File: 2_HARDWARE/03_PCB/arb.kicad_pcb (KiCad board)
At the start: 6 copper layers, 104.3 x 53.5 mm, 269 parts, among them J1 TYPE-C-31-M-12, J2 SMA, J3 SMA, J4 BNC, J5 PH-00244, SW1 TS-1187A-B-A-B, U1 TLV70333DBV, U10 LMK1C1103PWR, U11 STM32F446ZETx, U12 ICE40UP5K-SG48ITR, U13 93LC56BT-I_OT, U14 FT2232HL, U15 W25Q128JVSIQ, U16 W25Q128JVSIQ, U17 AD9850, U18 AD9744, U19 LM6171, U2 TLV76133DCY, U20 LM6171, U21 TMUX6104, U22 TPL0401B-10, U23 THS3491, U24 ADG1219BRJZ, U25 LM6171, U26 TMUX6104, U3 TLV70333DBV, U4 LM3880MF-1AA, U5 TLV70312DBV, U6 TLV70325DBV, U7 TPS65131RGE, U8 TPD2E001DRL, U9 ADG1219BRJZ, X1 ASE-10.000MHz, X2 ASE-100.000MHz, Y1 32.768k, Y2 12 MHz

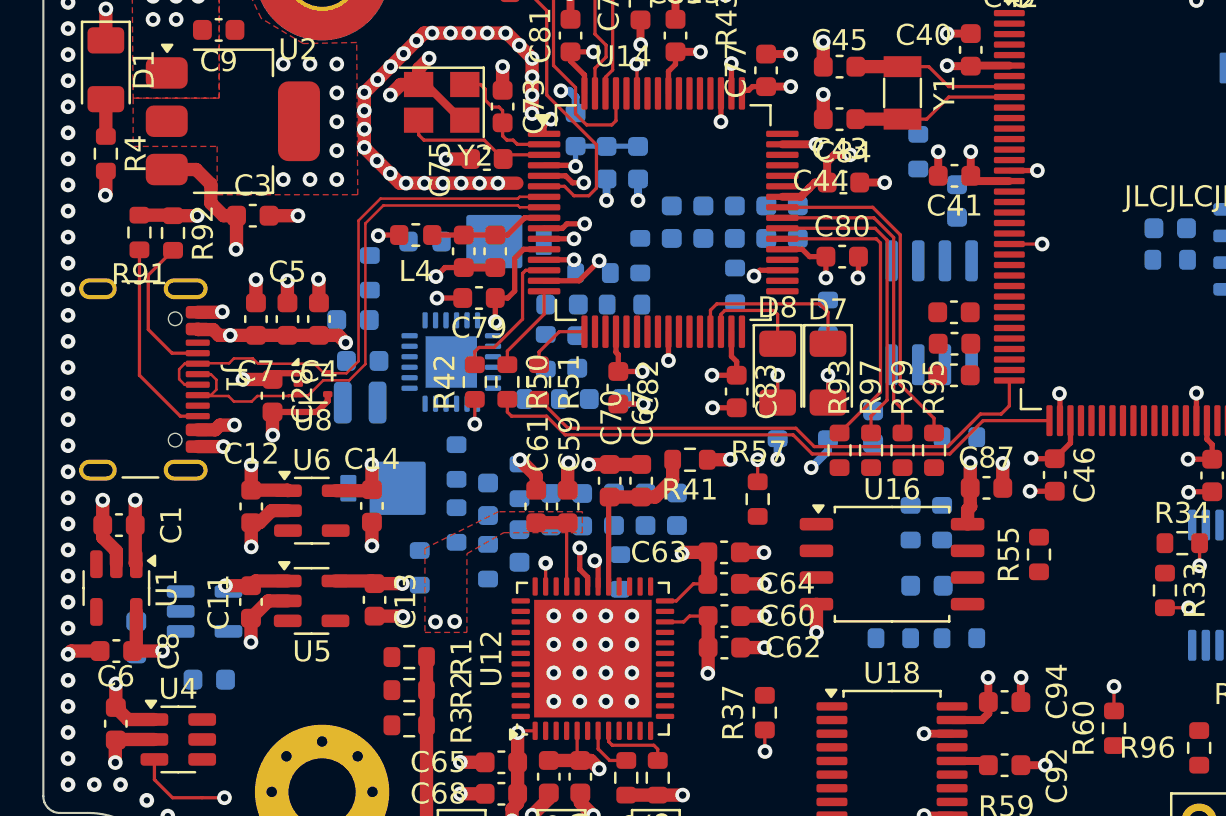
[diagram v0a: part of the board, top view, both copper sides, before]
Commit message: MINOR: Added missing vias, started on BS Routing.
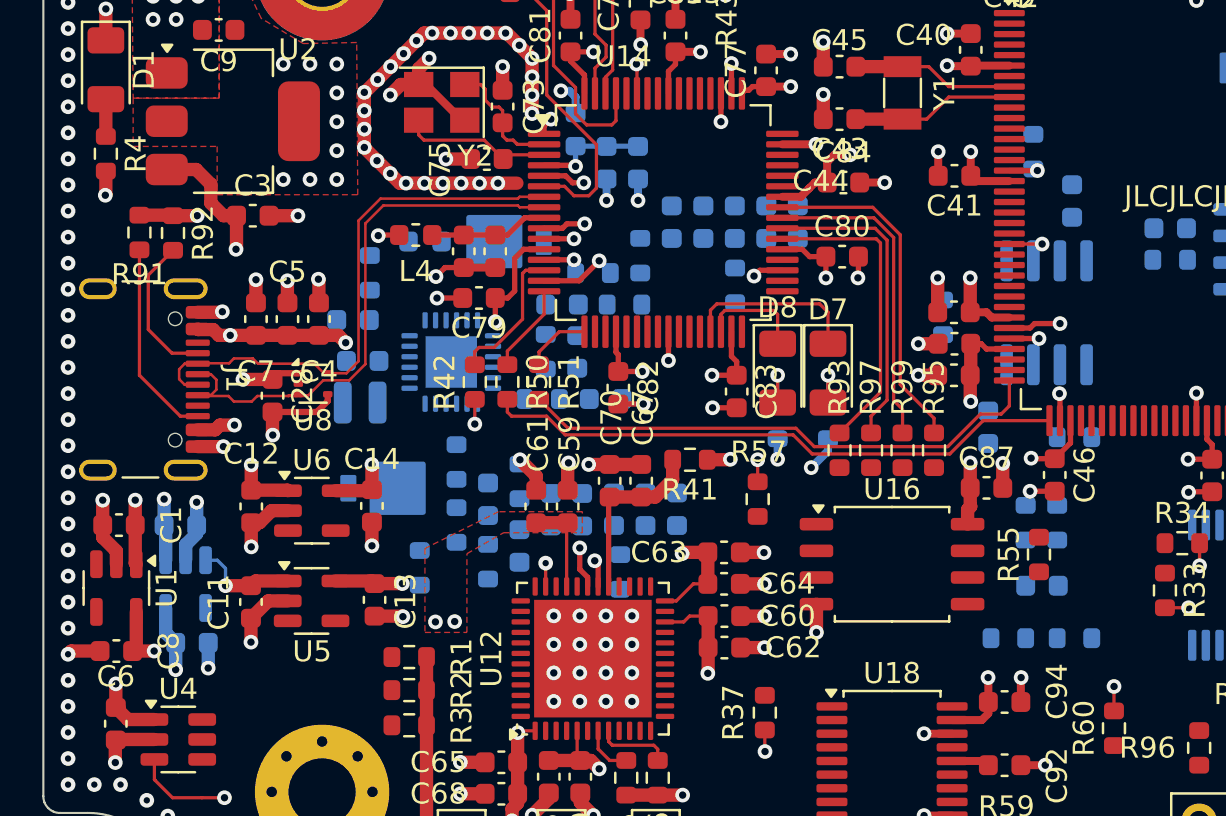
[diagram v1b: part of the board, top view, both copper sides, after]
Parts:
- moved C2 5.75 mm to (102.3, 93.7), turned to 0 degrees
- moved R65 5.48 mm to (142.6, 93.6)
- moved R66 5.48 mm to (144.1, 93.6)
- moved R71 5.48 mm to (138.7, 83.8)
- moved U19 5.48 mm to (143.6, 83.6)
- moved C95 5.48 mm to (143.4, 96.6)
- moved C97 5.48 mm to (144.8, 78.2)
- moved C99 5.48 mm to (140.8, 89.0)
- moved R61 5.48 mm to (141.8, 99.1)
- moved R63 5.48 mm to (144.9, 99.1)
- moved R69 5.48 mm to (144.9, 89.5)
- moved R73 5.48 mm to (143.0, 75.9)
- moved C10 1.93 mm to (102.9, 99.3), turned to 0 degrees
- moved U3 1.58 mm to (102.6, 96.5), turned to -90 degrees
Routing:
- net GND: track 193.5 -> 203.7 mm, vias 383 -> 389
- net 3P3V_A: track 8.92 -> 17.2 mm, vias 2 -> 4
- net 3P3V_D: track 125.2 -> 130.2 mm, vias 60 -> 62
- net 5P0V: track 33.2 -> 38.1 mm, vias 11 -> 12
- added copper zone on In3.Cu, net 3P3V_A

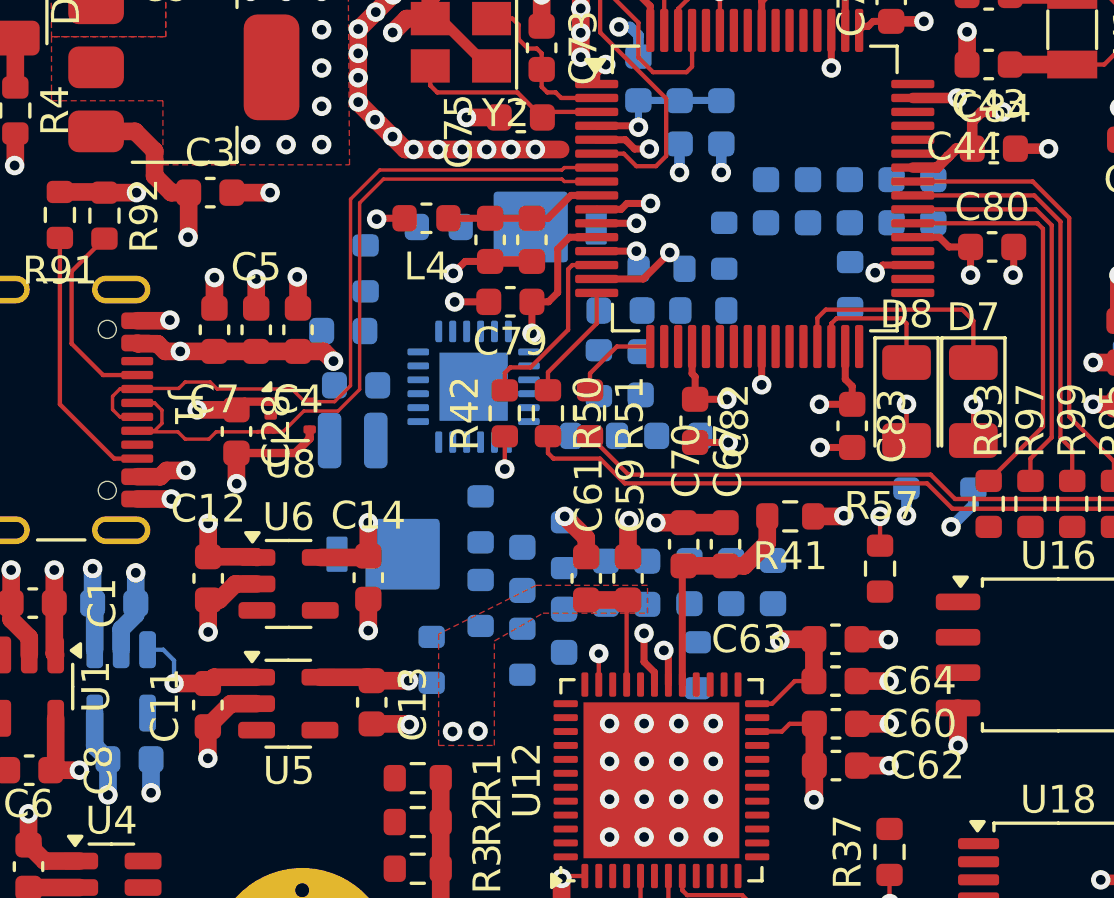
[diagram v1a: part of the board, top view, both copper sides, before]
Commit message: MINOR: Adjusted Fill Clearances to 10 mil, continued with +/-15V Regulator Layout. Added First VIA in Pad.
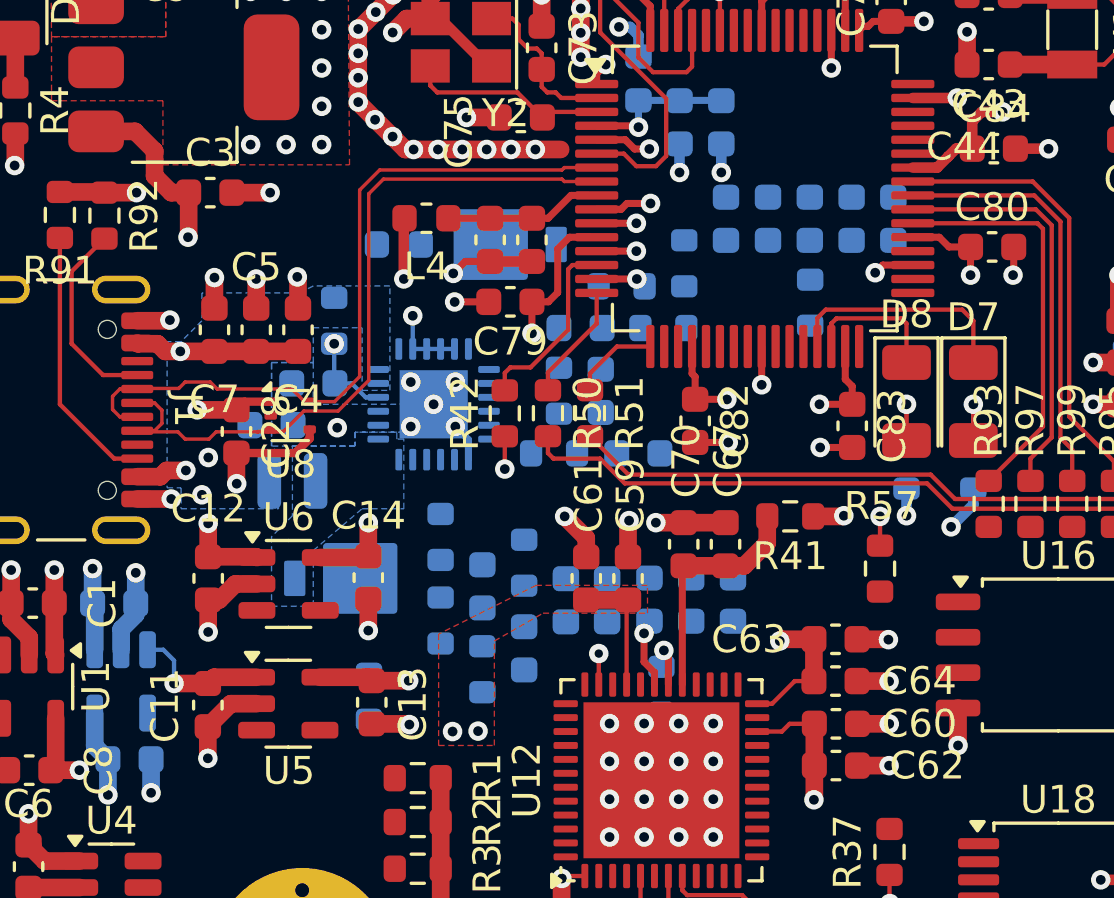
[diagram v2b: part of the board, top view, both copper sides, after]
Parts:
- moved C15 3.36 mm to (108.0, 87.3)
- moved R7 2.61 mm to (111.5, 97.0)
- moved L1 2.61 mm to (108.8, 89.3)
- moved R5 2.19 mm to (110.2, 83.5)
- moved C16 2.17 mm to (109.5, 85.8)
- moved D2 1.75 mm to (110.5, 92.8)
- moved R16 1.57 mm to (122.0, 96.8)
- moved C19 1.57 mm to (115.6, 93.1)
- moved C22 1.57 mm to (118.6, 93.6)
- moved C23 1.57 mm to (124.3, 79.9)
- moved C25 1.57 mm to (125.8, 79.9)
- moved C30 1.57 mm to (128.8, 79.9)
- moved C31 1.57 mm to (120.0, 93.6)
- moved C32 1.57 mm to (130.3, 79.9)
- moved R17 1.57 mm to (127.3, 82.9)
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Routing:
- net Net-(U7-ENN): track 0.00 -> 9.13 mm, vias 0 -> 2
- net 5P0V: track 38.1 -> 36.7 mm, vias 12 -> 13
- net 3P3V_D: track 130.2 -> 131.4 mm
- net GND: track 203.7 -> 203.9 mm, vias 389 -> 395
- added copper zone on B.Cu, net 5P0V
- added copper zone on B.Cu, net GND
- added copper zone on B.Cu, net Net-(D2-A)

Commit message: FEAT: Laid out +/-15V Regulator. Fixed input resistor into +/-15V Regulator Power. Named Power Planes.
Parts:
- R5: value 110k -> 100
- moved R17 7.19 mm to (134.2, 80.8), turned to 180 degrees
- moved R16 5.82 mm to (126.8, 93.5), turned to 180 degrees
- moved R7 5.71 mm to (117.1, 98.3)
- moved L2 5.70 mm to (118.2, 79.8), turned to 180 degrees
- moved R14 3.72 mm to (121.9, 87.5), turned to -90 degrees
- moved R13 3.57 mm to (123.3, 84.5), turned to -90 degrees
- moved C21 2.88 mm to (121.9, 84.5), turned to -90 degrees
- moved C23 2.32 mm to (126.0, 81.5), turned to -90 degrees
- moved C30 2.32 mm to (130.5, 81.5), turned to -90 degrees
- moved C32 2.32 mm to (132.0, 81.5), turned to -90 degrees
- moved C25 2.32 mm to (127.5, 81.5), turned to -90 degrees
- moved C27 2.32 mm to (129.0, 81.5), turned to -90 degrees
- moved R15 1.65 mm to (124.5, 81.5)
- moved D3 1.43 mm to (117.4, 82.0)
- moved C18 1.11 mm to (120.4, 89.1), turned to -90 degrees
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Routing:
- net Net-(D2-K): track 0.00 -> 30.4 mm
- net Net-(D3-A): track 0.00 -> 21.1 mm
- net Net-(U7-FBN): track 0.00 -> 9.90 mm
- net Net-(R13-Pad2): track 0.00 -> 8.05 mm
- net Net-(U7-FBP): track 0.00 -> 6.67 mm
- net GND: track 203.9 -> 208.9 mm, vias 395 -> 399
- net Net-(U7-CP): track 0.00 -> 4.85 mm
- net Net-(R11-Pad1): track 0.00 -> 4.78 mm
- net Net-(U7-VREF): track 0.00 -> 4.20 mm
- net 1P8V_D: track 14.1 -> 17.1 mm
- net Net-(U7-CN): track 0.00 -> 1.72 mm
- net Net-(C17-Pad1): track 0.00 -> 1.47 mm
- net Net-(C18-Pad1): track 0.00 -> 1.41 mm
- net Net-(C21-Pad2): track 0.00 -> 1.38 mm
- net Net-(C19-Pad1): track 0.00 -> 1.38 mm
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- added copper zone on B.Cu, net 15P0V_A
- added copper zone on In3.Cu, net 1P8V_D
- added copper zone on B.Cu, net N15P0V_A
- added copper zone on B.Cu, net Net-(D3-K)

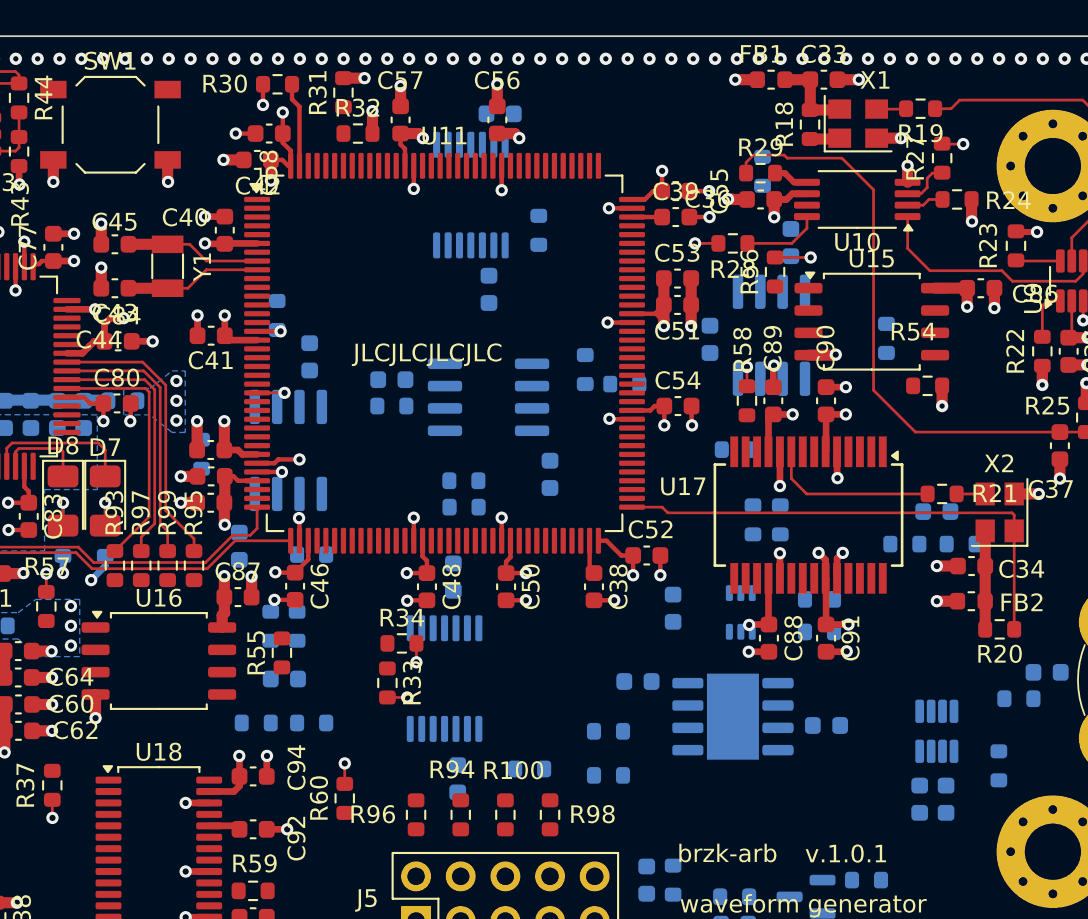
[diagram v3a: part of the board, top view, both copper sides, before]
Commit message: MINOR: Moved Analog Components for easier routing.
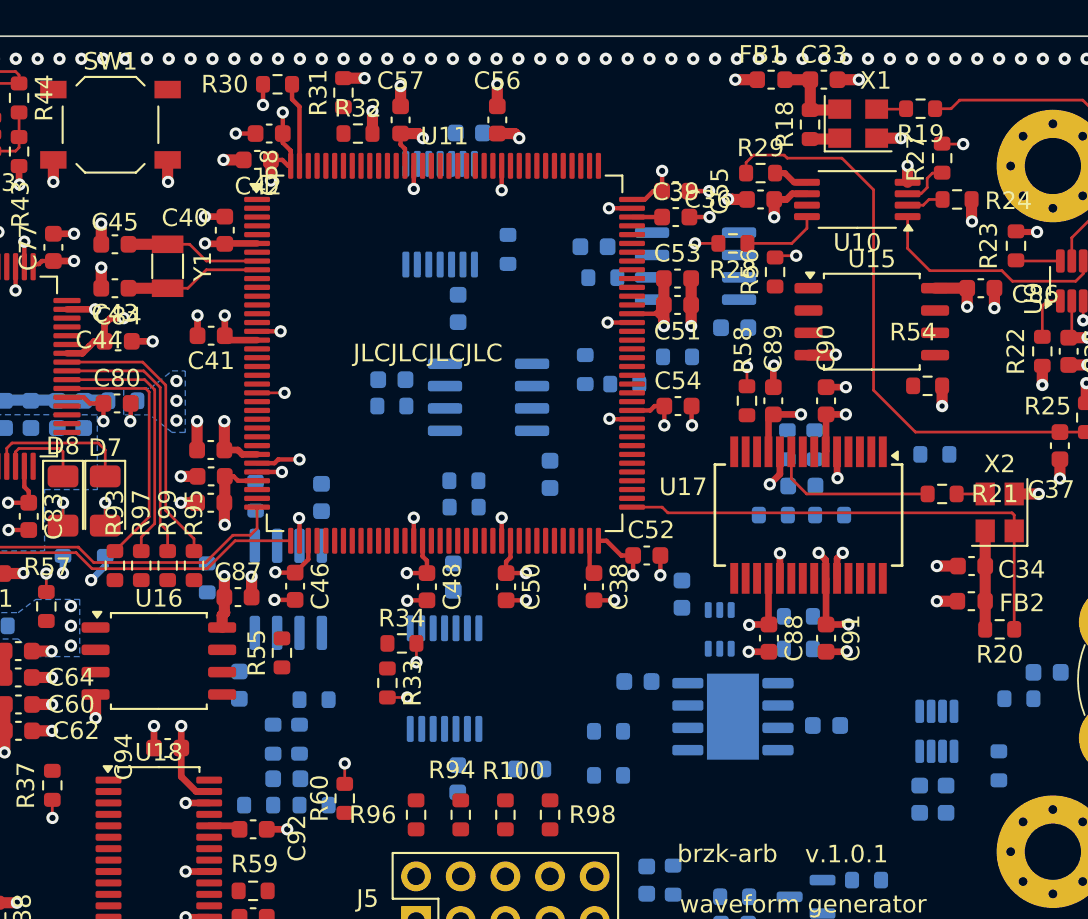
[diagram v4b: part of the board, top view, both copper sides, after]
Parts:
- moved R72 11.9 mm to (165.8, 78.2), turned to 180 degrees
- moved R70 11.3 mm to (180.4, 83.8)
- moved C98 11.2 mm to (161.0, 72.0), turned to 180 degrees
- moved R74 10.9 mm to (161.5, 73.8), turned to 180 degrees
- moved R73 10.3 mm to (141.8, 86.2)
- moved R69 8.25 mm to (145.1, 97.8)
- moved C97 8.03 mm to (145.5, 86.2)
- moved C99 7.90 mm to (140.8, 96.9)
- moved U19 7.90 mm to (143.6, 91.5)
- moved C96 7.82 mm to (172.8, 85.6)
- moved R64 7.66 mm to (171.2, 87.2)
- moved R62 7.66 mm to (174.4, 87.2)
- moved R71 7.04 mm to (139.0, 90.8)
- moved R65 6.43 mm to (142.8, 100.0)
- moved R66 6.43 mm to (144.2, 100.0)
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
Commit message: FEAT: Completed Power Planes, GND, and Analog Placement.
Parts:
- moved C110 2.26 mm to (184.8, 95.2), turned to 0 degrees
- moved R84 1.14 mm to (184.8, 96.6)
- moved R17 1.12 mm to (133.5, 79.9), turned to -90 degrees
- moved C101 1.03 mm to (153.2, 64.7), turned to 90 degrees
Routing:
- net N15P0V_A: track 0.07 -> 102.1 mm, vias 3 -> 12
- net 15P0V_A: track 0.00 -> 92.3 mm, vias 3 -> 11
- net GND: track 209.1 -> 260.7 mm, vias 399 -> 443
- net 3P3V_A: track 17.6 -> 32.2 mm, vias 4 -> 7
- net 3P3V_D: track 131.5 -> 139.1 mm, vias 62 -> 64
- net GPIO_EN_MCU_AMUX3_3P3: track 0.00 -> 5.52 mm, vias 0 -> 1
- added copper zone on In2.Cu, net 15P0V_A
- added copper zone on In2.Cu, net N15P0V_A
